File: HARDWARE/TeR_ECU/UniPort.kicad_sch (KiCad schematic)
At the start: 1 part, among them J1 RJ45_Shielded

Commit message: Empezado el Layout
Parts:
- J1: footprint (none) -> Connector_RJ:RJ45_Ninigi_GE
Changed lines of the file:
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@@
       (effects (font (size 1.27 1.27)))
     )
-    (property "Footprint" "" (at 127 86.995 90)
+    (property "Footprint" "Connector_RJ:RJ45_Ninigi_GE" (at 127 86.995 90)
       (effects (font (size 1.27 1.27)) hide)
     )

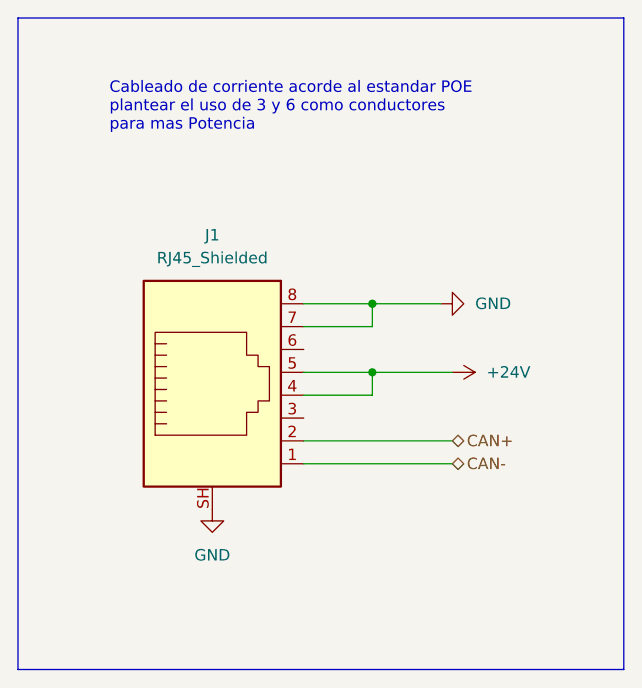
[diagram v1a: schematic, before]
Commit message: Rethought layout and footprints and fixed fuse normative problem
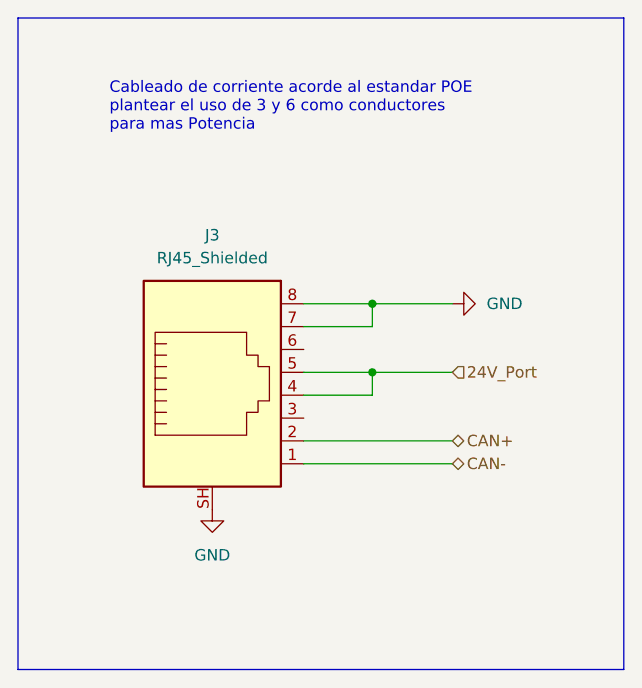
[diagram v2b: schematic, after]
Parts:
- renumbered J1 to J3
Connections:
- net +24V renamed 24V_Port
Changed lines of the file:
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@@
     (stroke (width 0) (type default))
   )
-  (wire (pts (xy 144.78 77.47) (xy 152.4 77.47))
+  (wire (pts (xy 144.78 77.47) (xy 153.67 77.47))
     (stroke (width 0) (type default))
   )
@@
     (effects (font (size 1.27 1.27)) (justify left bottom))
   )
+  (hierarchical_label "24V_Port" (shape input) (at 153.67 85.09 0) (fields_autoplaced)
+    (effects (font (size 1.27 1.27)) (justify left))
+  )
   (hierarchical_label "CAN+" (shape bidirectional) (at 153.67 92.71 0) (fields_autoplaced)
     (effects (font (size 1.27 1.27)) (justify left))
@@
     (effects (font (size 1.27 1.27)) (justify left))
   )
-  (symbol (lib_id "power:+24V") (at 153.67 85.09 270) (unit 1)
+  (symbol (lib_id "power:GND") (at 153.67 77.47 90) (unit 1)
     (in_bom yes) (on_board yes) (dnp no) (fields_autoplaced)
-    (property "Reference" "#PWR012" (at 149.86 85.09 0)
+    (property "Reference" "#PWR035" (at 160.02 77.47 0)
       (effects (font (size 1.27 1.27)) hide)
     )
-    (property "Value" "+24V" (at 157.48 85.09 90)
-      (effects (font (size 1.27 1.27)) (justify left))
+    (property "Value" "GND" (at 157.48 77.47 90)
+      (effects (font (size 1.27 1.27)) (justify right))
     )
-    (property "Footprint" "" (at 153.67 85.09 0)
+    (property "Footprint" "" (at 153.67 77.47 0)
       (effects (font (size 1.27 1.27)) hide)
     )
-    (property "Datasheet" "" (at 153.67 85.09 0)
+    (property "Datasheet" "" (at 153.67 77.47 0)
       (effects (font (size 1.27 1.27)) hide)
     )
@@
       (project "TeR_ECU"
         (path "/84413845-c4f3-4743-bcd2-a67649c90902/c9231e89-0d66-4ea8-9e74-d5a61fdabf8a"
-          (reference "#PWR012") (unit 1)
+          (reference "#PWR035") (unit 1)
         )
         (path "/84413845-c4f3-4743-bcd2-a67649c90902/89fa6b65-e09d-462b-a9d8-e2037e38fa73"
-          (reference "#PWR039") (unit 1)
+          (reference "#PWR028") (unit 1)
         )
         (path "/84413845-c4f3-4743-bcd2-a67649c90902/b3d71585-a15b-4975-adfa-12ed469b60dd"
-          (reference "#PWR045") (unit 1)
-        )
-      )
-    )
-  )
-  (symbol (lib_id "power:GND") (at 152.4 77.47 90) (unit 1)
-    (in_bom yes) (on_board yes) (dnp no) (fields_autoplaced)
-    (property "Reference" "#PWR011" (at 158.75 77.47 0)
-      (effects (font (size 1.27 1.27)) hide)
-    )
-    (property "Value" "GND" (at 156.21 77.47 90)
-      (effects (font (size 1.27 1.27)) (justify right))
-    )
-    (property "Footprint" "" (at 152.4 77.47 0)
-      (effects (font (size 1.27 1.27)) hide)
-    )
-    (property "Datasheet" "" (at 152.4 77.47 0)
-      (effects (font (size 1.27 1.27)) hide)
-    )
-    (pin "1")
-    (instances
-      (project "TeR_ECU"
-        (path "/84413845-c4f3-4743-bcd2-a67649c90902/c9231e89-0d66-4ea8-9e74-d5a61fdabf8a"
-          (reference "#PWR011") (unit 1)
-        )
-        (path "/84413845-c4f3-4743-bcd2-a67649c90902/89fa6b65-e09d-462b-a9d8-e2037e38fa73"
-          (reference "#PWR019") (unit 1)
-        )
-        (path "/84413845-c4f3-4743-bcd2-a67649c90902/b3d71585-a15b-4975-adfa-12ed469b60dd"
-          (reference "#PWR043") (unit 1)
+          (reference "#PWR037") (unit 1)
         )
       )
@@
   (symbol (lib_id "power:GND") (at 127 100.33 0) (unit 1)
     (in_bom yes) (on_board yes) (dnp no) (fields_autoplaced)
-    (property "Reference" "#PWR013" (at 127 106.68 0)
+    (property "Reference" "#PWR036" (at 127 106.68 0)
       (effects (font (size 1.27 1.27)) hide)
     )
@@
       (project "TeR_ECU"
         (path "/84413845-c4f3-4743-bcd2-a67649c90902/c9231e89-0d66-4ea8-9e74-d5a61fdabf8a"
-          (reference "#PWR013") (unit 1)
+          (reference "#PWR036") (unit 1)
         )
         (path "/84413845-c4f3-4743-bcd2-a67649c90902/89fa6b65-e09d-462b-a9d8-e2037e38fa73"
-          (reference "#PWR017") (unit 1)
+          (reference "#PWR029") (unit 1)
         )
         (path "/84413845-c4f3-4743-bcd2-a67649c90902/b3d71585-a15b-4975-adfa-12ed469b60dd"
-          (reference "#PWR041") (unit 1)
+          (reference "#PWR038") (unit 1)
         )
       )
@@
   (symbol (lib_id "Connector:RJ45_Shielded") (at 127 87.63 0) (unit 1)
     (in_bom yes) (on_board yes) (dnp no) (fields_autoplaced)
-    (property "Reference" "J1" (at 127 69.85 0)
+    (property "Reference" "J3" (at 127 69.85 0)
       (effects (font (size 1.27 1.27)))
     )
@@
       (project "TeR_ECU"
         (path "/84413845-c4f3-4743-bcd2-a67649c90902/c9231e89-0d66-4ea8-9e74-d5a61fdabf8a"
-          (reference "J1") (unit 1)
+          (reference "J3") (unit 1)
         )
         (path "/84413845-c4f3-4743-bcd2-a67649c90902/89fa6b65-e09d-462b-a9d8-e2037e38fa73"
@@
         )
         (path "/84413845-c4f3-4743-bcd2-a67649c90902/b3d71585-a15b-4975-adfa-12ed469b60dd"
-          (reference "J3") (unit 1)
+          (reference "J4") (unit 1)
         )
       )

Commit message: Updated UNIPORT to fit the new 3 and 6 pin connected to PWR
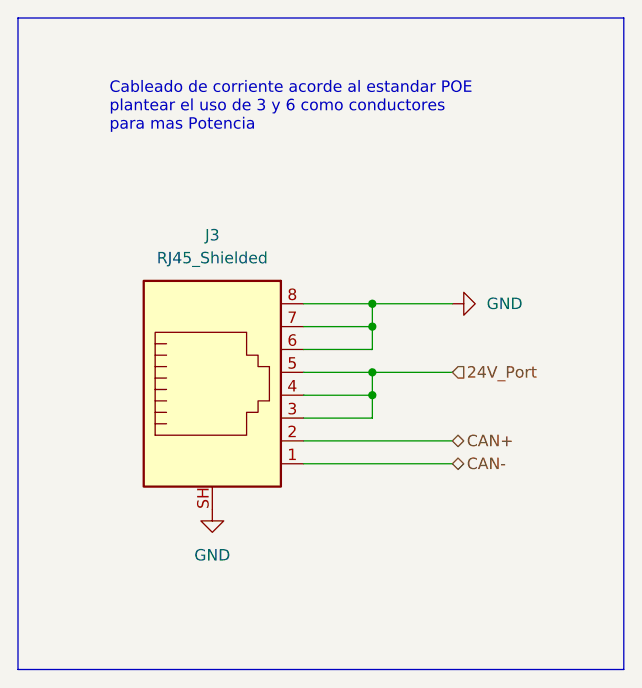
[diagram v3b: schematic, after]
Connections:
- net 24V_Port: now also J3.3
- net GND: now also J3.6
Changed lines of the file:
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@@
 (kicad_sch (version 20230121) (generator eeschema)
   (paper "A4")
+  (junction (at 144.78 80.01) (diameter 0) (color 0 0 0 0)
+  )
+  (junction (at 144.78 87.63) (diameter 0) (color 0 0 0 0)
+  )
   (junction (at 144.78 85.09) (diameter 0) (color 0 0 0 0)
   )
@@
     (stroke (width 0) (type default))
   )
+  (wire (pts (xy 144.78 80.01) (xy 144.78 82.55))
+    (stroke (width 0) (type default))
+  )
   (wire (pts (xy 137.16 87.63) (xy 144.78 87.63))
     (stroke (width 0) (type default))
@@
     (stroke (width 0) (type default))
   )
+  (wire (pts (xy 137.16 90.17) (xy 144.78 90.17))
+    (stroke (width 0) (type default))
+  )
   (wire (pts (xy 137.16 77.47) (xy 144.78 77.47))
     (stroke (width 0) (type default))
   )
+  (wire (pts (xy 144.78 90.17) (xy 144.78 87.63))
+    (stroke (width 0) (type default))
+  )
   (wire (pts (xy 137.16 80.01) (xy 144.78 80.01))
+    (stroke (width 0) (type default))
+  )
+  (wire (pts (xy 137.16 82.55) (xy 144.78 82.55))
     (stroke (width 0) (type default))
   )
@@
     (stroke (width 0) (type default))
   )
-  (wire (pts (xy 144.78 80.01) (xy 144.78 77.47))
+  (wire (pts (xy 144.78 77.47) (xy 144.78 80.01))
     (stroke (width 0) (type default))
   )

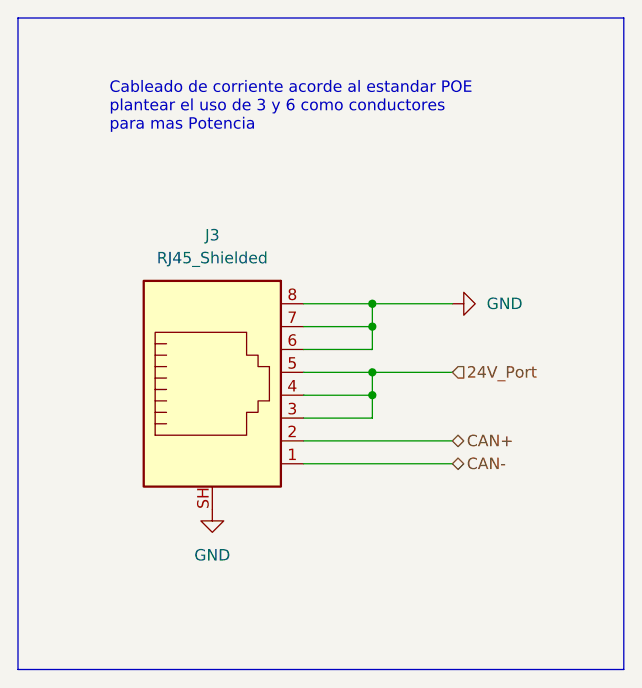
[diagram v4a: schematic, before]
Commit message: usb-c, good debug conn, switch
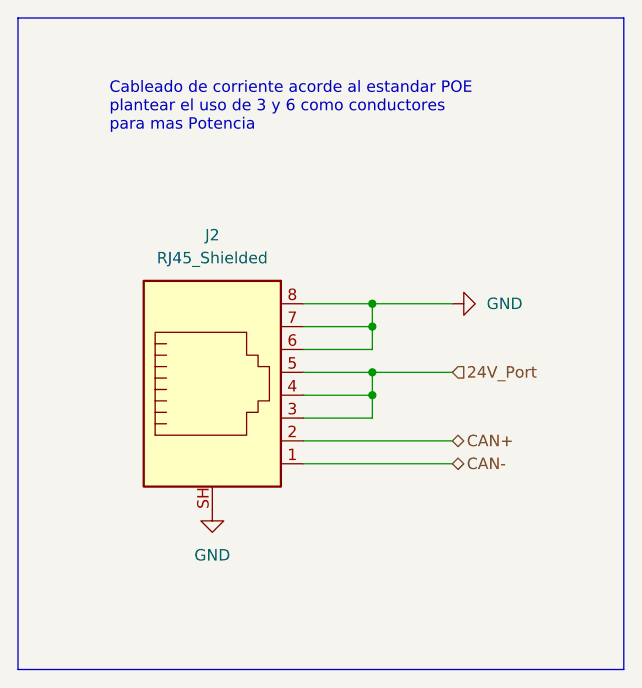
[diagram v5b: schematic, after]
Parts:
- renumbered J3 to J2

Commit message: Kept improving schmatic for V2
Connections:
- net 24V_Port renamed 24_VIN
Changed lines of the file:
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@@
 		)
 	)
-	(hierarchical_label "24V_Port"
+	(global_label "24_VIN"
 		(shape input)
 		(at 153.67 85.09 0)
@@
 			(justify left)
 		)
+		(property "Intersheetrefs" "${INTERSHEET_REFS}"
+			(at 163.0657 85.09 0)
+			(effects
+				(font
+					(size 1.27 1.27)
+				)
+				(justify left)
+				(hide yes)
+			)
+		)
 	)

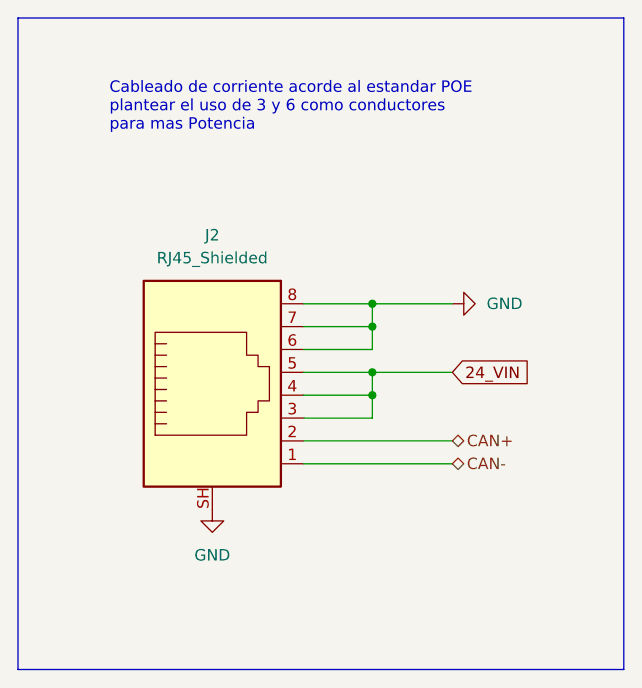
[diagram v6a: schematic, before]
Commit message: Advanced design and added IMU/GPS moduleç
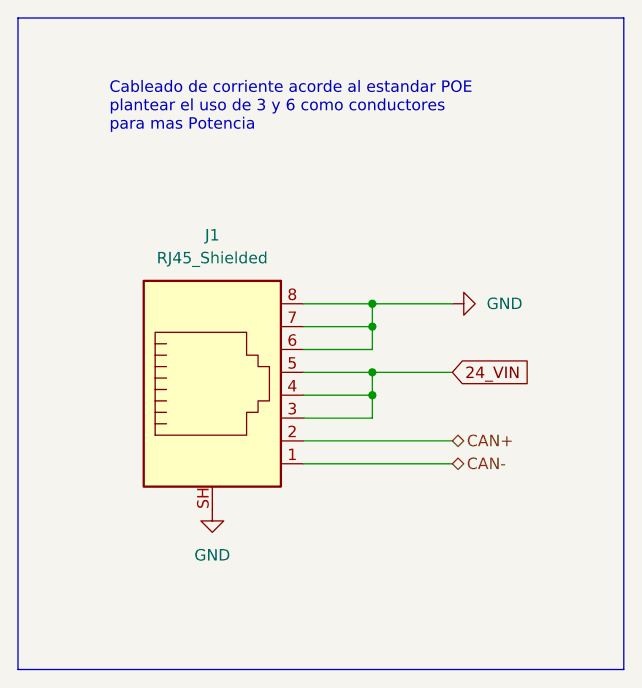
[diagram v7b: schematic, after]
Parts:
- renumbered J2 to J1
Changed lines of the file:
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@@
 		(dnp no)
 		(fields_autoplaced yes)
-		(property "Reference" "#PWR028"
+		(property "Reference" "#PWR016"
 			(at 160.02 77.47 0)
 			(effects
@@
 			(project "TeR_ECU"
 				(path "/84413845-c4f3-4743-bcd2-a67649c90902/89fa6b65-e09d-462b-a9d8-e2037e38fa73"
-					(reference "#PWR028")
+					(reference "#PWR016")
 					(unit 1)
 				)
 				(path "/84413845-c4f3-4743-bcd2-a67649c90902/b3d71585-a15b-4975-adfa-12ed469b60dd"
-					(reference "#PWR037")
+					(reference "#PWR025")
 					(unit 1)
 				)
@@
 		(dnp no)
 		(fields_autoplaced yes)
-		(property "Reference" "#PWR029"
+		(property "Reference" "#PWR017"
 			(at 127 106.68 0)
 			(effects
@@
 			(project "TeR_ECU"
 				(path "/84413845-c4f3-4743-bcd2-a67649c90902/89fa6b65-e09d-462b-a9d8-e2037e38fa73"
-					(reference "#PWR029")
+					(reference "#PWR017")
 					(unit 1)
 				)
 				(path "/84413845-c4f3-4743-bcd2-a67649c90902/b3d71585-a15b-4975-adfa-12ed469b60dd"
-					(reference "#PWR038")
+					(reference "#PWR026")
 					(unit 1)
 				)
@@
 		(dnp no)
 		(fields_autoplaced yes)
-		(property "Reference" "J2"
+		(property "Reference" "J1"
 			(at 127 69.85 0)
 			(effects
@@
 			(project "TeR_ECU"
 				(path "/84413845-c4f3-4743-bcd2-a67649c90902/89fa6b65-e09d-462b-a9d8-e2037e38fa73"
+					(reference "J1")
+					(unit 1)
+				)
+				(path "/84413845-c4f3-4743-bcd2-a67649c90902/b3d71585-a15b-4975-adfa-12ed469b60dd"
 					(reference "J2")
 					(unit 1)
 				)
-				(path "/84413845-c4f3-4743-bcd2-a67649c90902/b3d71585-a15b-4975-adfa-12ed469b60dd"
-					(reference "J4")
-					(unit 1)
-				)
